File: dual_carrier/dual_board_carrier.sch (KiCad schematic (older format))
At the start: 28 parts, among them J1 Conn_01x08, J2 Conn_01x08, J3 Conn_02x10_Top_Bottom, J4 Conn_01x08, J5 Conn_01x08, U1 TJA1051T-3, U2 LM78M05_TO252, U3 TJA1051T-3

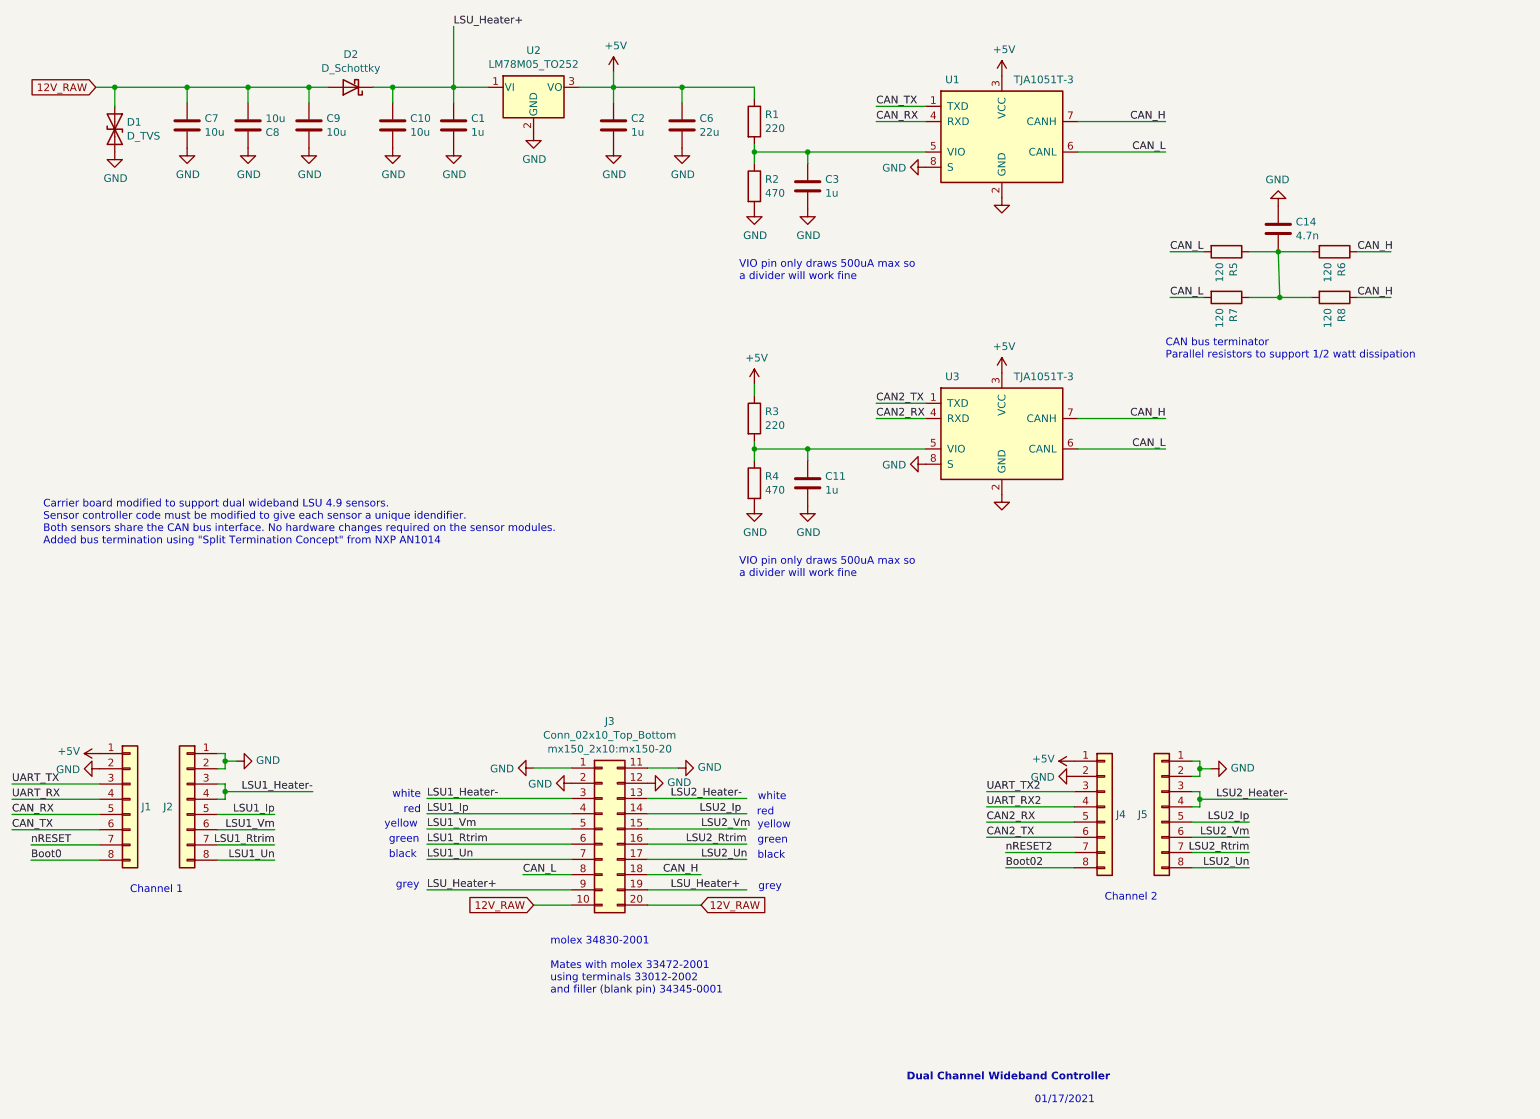
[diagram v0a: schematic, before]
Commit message: Add files via upload
02/07/21 Updates to dual_carrier and creation of dual_carrier_sxs
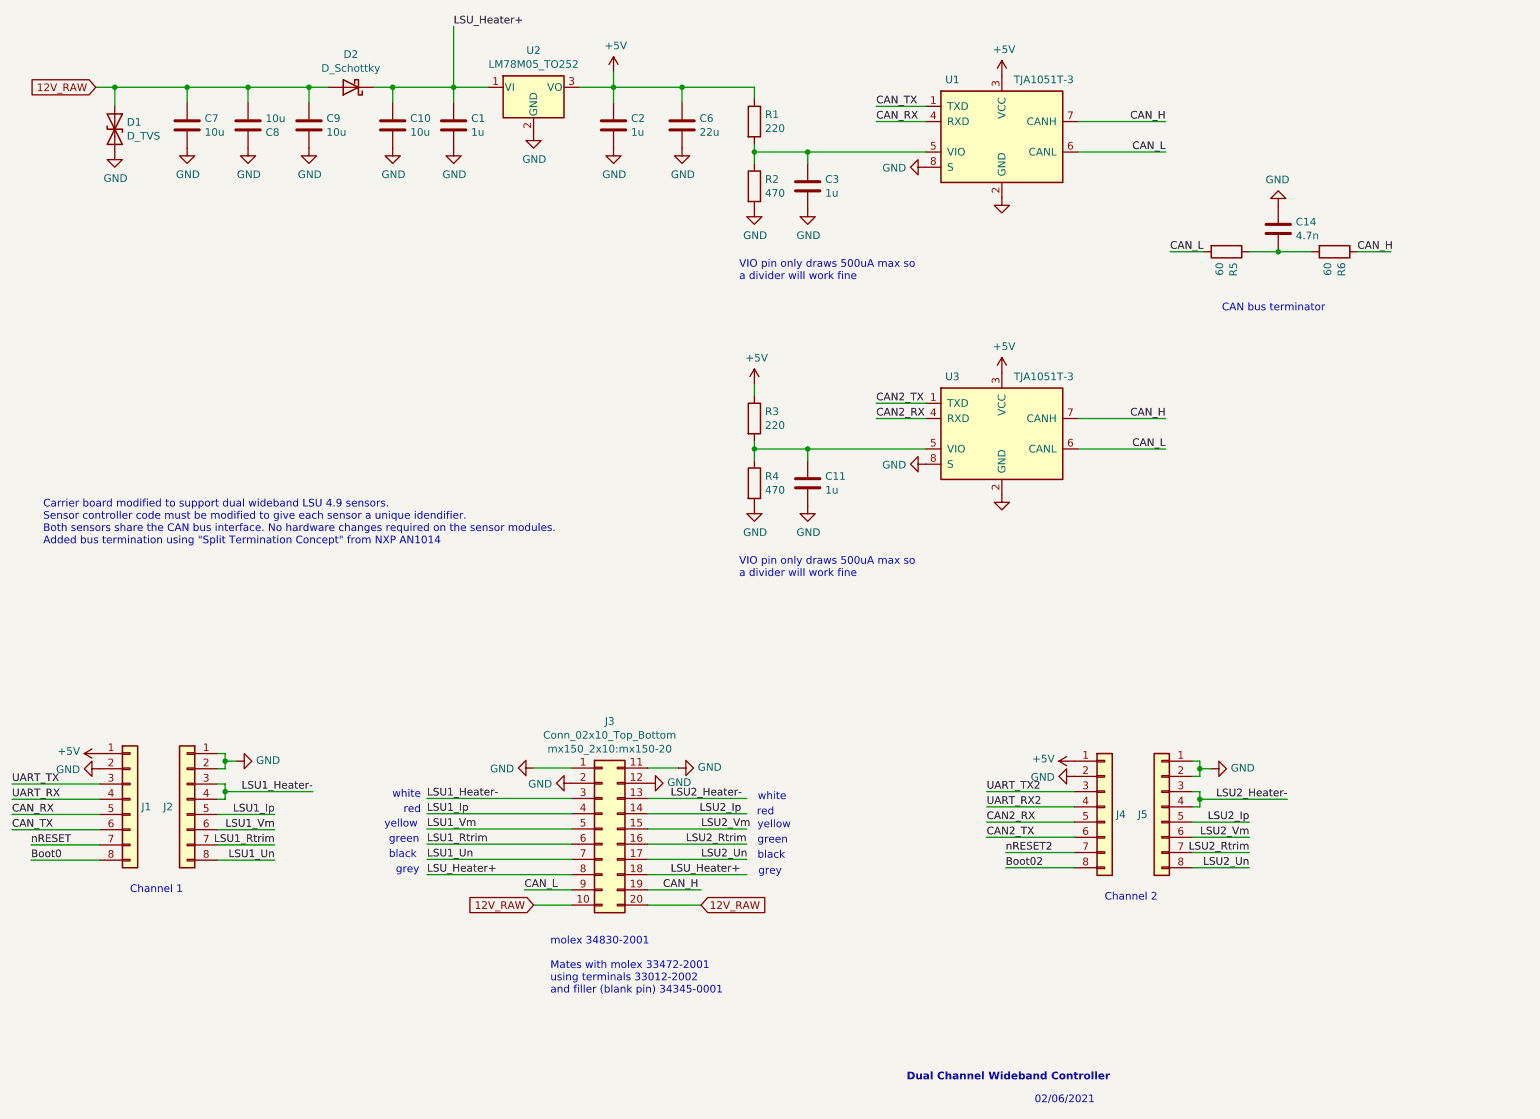
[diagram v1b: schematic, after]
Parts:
- removed R7, R8: 120, Resistor_SMD:R_1206_3216Metric, symbol Device:R
- R5, R6: value 120 -> 60
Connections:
- wire segments 108 -> 103
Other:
- note added: "02/06/2021"
- note added: "CAN bus terminator"
- note removed: "01/17/2021"
- note removed: "CAN bus terminator\nParallel resistors to support 1/2 watt dissipation"
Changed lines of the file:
@@
 	1    0    0    -1
 $EndComp
-Text Notes 3450 6470 2    50   ~ 0
+Text Notes 3450 6370 2    50   ~ 0
 grey
 Text Notes 3460 5875 2    50   ~ 0
@@
 	4450 5870 3500 5870
 Wire Wire Line
-	4450 6470 3500 6470
-Wire Wire Line
 	4450 6070 3500 6070
 Wire Wire Line
@@
 	4950 5870 5600 5870
 Wire Wire Line
-	4950 6470 5600 6470
+	4950 6370 5600 6370
 Wire Wire Line
 	4950 6070 5600 6070
@@
 	4950 5670 5150 5670
 Wire Wire Line
-	4950 6370 5300 6370
+	4950 6470 5300 6470
 Text Label 3500 5970 0    50   ~ 0
 LSU1_Ip
 Text Label 3500 5870 0    50   ~ 0
 LSU1_Heater-
-Text Label 3500 6470 0    50   ~ 0
+Text Label 3500 6370 0    50   ~ 0
 LSU_Heater+
 Text Label 3500 6070 0    50   ~ 0
@@
 Text Label 3500 6270 0    50   ~ 0
 LSU1_Un
-Text Label 5050 6370 0    50   ~ 0
+Text Label 5050 6470 0    50   ~ 0
 CAN_H
-Text Label 4130 6370 0    50   ~ 0
+Text Label 4140 6470 0    50   ~ 0
 CAN_L
 Text Label 5290 5970 0    50   ~ 0
@@
 Text Label 5100 5870 0    50   ~ 0
 LSU2_Heater-
-Text Label 5100 6470 0    50   ~ 0
+Text Label 5100 6370 0    50   ~ 0
 LSU_Heater+
 Text Label 5300 6070 0    50   ~ 0
@@
 Text Notes 3220 6070 0    50   ~ 0
 yellow
-Text Notes 5830 6480 2    50   ~ 0
+Text Notes 5830 6380 2    50   ~ 0
 grey
 Text Notes 5860 5890 2    50   ~ 0
@@
 Carrier board modified to support dual wideband LSU 4.9 sensors.\nSensor controller code must be modified to give each sensor a unique idendifier.\nBoth sensors share the CAN bus interface. No hardware changes required on the sensor modules.\nAdded bus termination using "Split Termination Concept" from NXP AN1014
 Text Notes 7490 7880 0    50   ~ 0
-01/17/2021
+02/06/2021
 Text Notes 6650 7730 0    50   ~ 10
 Dual Channel Wideband Controller
@@
 P 8750 2280
 F 0 "R5" H 8820 2326 50  0000 L CNN
-F 1 "120" H 8820 2235 50  0000 L CNN
+F 1 "60" H 8820 2235 50  0000 L CNN
 F 2 "Resistor_SMD:R_1206_3216Metric" V 8680 2280 50  0001 C CNN
 F 3 "~" H 8750 2280 50  0001 C CNN
@@
 P 9460 2280
 F 0 "R6" H 9530 2326 50  0000 L CNN
-F 1 "120" H 9530 2235 50  0000 L CNN
+F 1 "60" H 9530 2235 50  0000 L CNN
 F 2 "Resistor_SMD:R_1206_3216Metric" V 9390 2280 50  0001 C CNN
 F 3 "~" H 9460 2280 50  0001 C CNN
@@
 $EndComp
 Wire Wire Line
-	4130 6370 4450 6370
+	4140 6470 4450 6470
 $Comp
 L power:GND #PWR0116
@@
 	0    -1   -1   0
 $EndComp
-$Comp
-L Device:R R7
-U 1 1 601867AB
-P 8750 2580
-F 0 "R7" H 8820 2626 50  0000 L CNN
-F 1 "120" H 8820 2535 50  0000 L CNN
-F 2 "Resistor_SMD:R_1206_3216Metric" V 8680 2580 50  0001 C CNN
-F 3 "~" H 8750 2580 50  0001 C CNN
-F 4 "C23179" H 8750 2580 50  0001 C CNN "LCSC"
-	1    8750 2580
-	0    1    1    0
-$EndComp
-$Comp
-L Device:R R8
-U 1 1 60186C0C
-P 9460 2580
-F 0 "R8" H 9530 2626 50  0000 L CNN
-F 1 "120" H 9530 2535 50  0000 L CNN
-F 2 "Resistor_SMD:R_1206_3216Metric" V 9390 2580 50  0001 C CNN
-F 3 "~" H 9460 2580 50  0001 C CNN
-F 4 "C23179" H 9460 2580 50  0001 C CNN "LCSC"
-	1    9460 2580
-	0    1    1    0
-$EndComp
-Wire Wire Line
-	8600 2580 8380 2580
-Wire Wire Line
-	9610 2580 9830 2580
-Text Label 9610 2580 0    50   ~ 0
-CAN_H
-Text Label 8380 2580 0    50   ~ 0
-CAN_L
-Wire Wire Line
-	8900 2580 9100 2580
-Wire Wire Line
-	9090 2280 9100 2580
-Connection ~ 9100 2580
-Wire Wire Line
-	9100 2580 9310 2580
-Text Notes 8350 2990 0    50   ~ 0
-CAN bus terminator\nParallel resistors to support 1/2 watt dissipation
+Text Notes 8720 2680 0    50   ~ 0
+CAN bus terminator
+Wire Wire Line
+	3500 6370 4450 6370
 $EndSCHEMATC
